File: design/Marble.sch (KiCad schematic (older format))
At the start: 20 parts

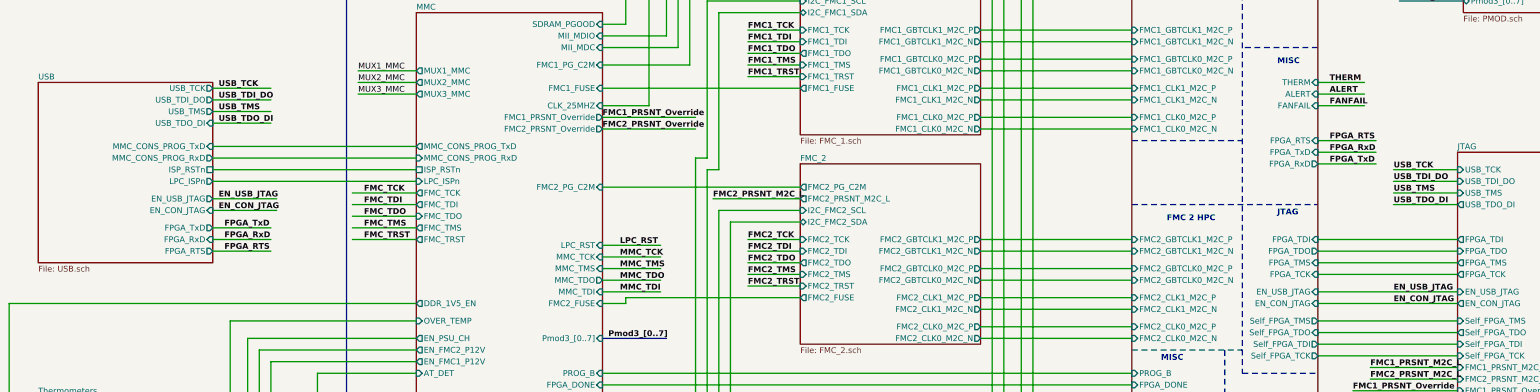
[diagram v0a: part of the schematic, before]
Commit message: buffering, solved ERC issues
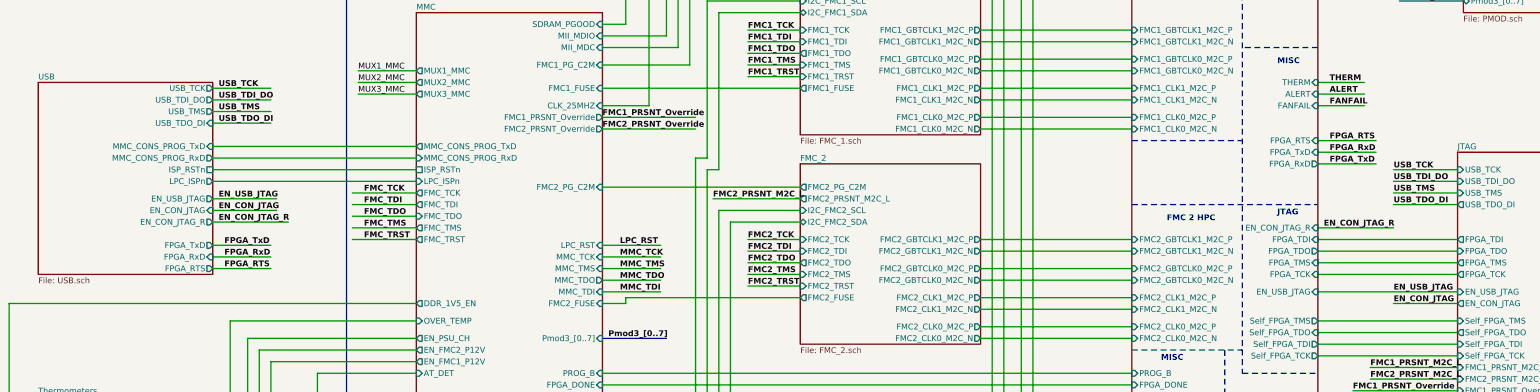
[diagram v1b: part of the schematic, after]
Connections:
- net labels added: EN_CON_JTAG_R
- wire segments 370 -> 372
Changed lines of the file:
@@
 $EndSheet
 $Sheet
-S 1950 7250 1500 1550
+S 1950 7250 1500 1650
 U 5C16C03C
 F0 "USB" 50
@@
 F9 "MMC_CONS_PROG_RxD" O R 3450 7900 50
 F10 "EN_CON_JTAG" I R 3450 8350 50
-F11 "FPGA_TxD" O R 3450 8500 50
-F12 "FPGA_RxD" I R 3450 8600 50
-F13 "FPGA_RTS" O R 3450 8700 50
+F11 "FPGA_TxD" O R 3450 8650 50
+F12 "FPGA_RxD" I R 3450 8750 50
+F13 "FPGA_RTS" O R 3450 8850 50
 F14 "ISP_RSTn" U R 3450 8000 50
+F15 "EN_CON_JTAG_R" O R 3450 8450 50
 $EndSheet
 Wire Wire Line
@@
 Wire Wire Line
 	12950 9050 14150 9050
-Wire Wire Line
-	12950 9150 14150 9150
 Text Label 6950 8650 0    50   ~ 10
 LPC_RST
@@
 Wire Wire Line
 	13450 7950 12950 7950
-Text Label 3550 8700 0    50   ~ 10
+Text Label 3550 8850 0    50   ~ 10
 FPGA_RTS
-Text Label 3550 8600 0    50   ~ 10
+Text Label 3550 8750 0    50   ~ 10
 FPGA_RxD
-Text Label 3550 8500 0    50   ~ 10
+Text Label 3550 8650 0    50   ~ 10
 FPGA_TxD
 Wire Wire Line
-	3950 8700 3450 8700
-Wire Wire Line
-	3950 8600 3450 8600
-Wire Wire Line
-	3950 8500 3450 8500
+	3950 8850 3450 8850
+Wire Wire Line
+	3950 8750 3450 8750
+Wire Wire Line
+	3950 8650 3450 8650
 Wire Wire Line
 	13400 9700 14150 9700
@@
 F58 "Self_FPGA_TDI" O R 12950 9500 50
 F59 "Self_FPGA_TCK" O R 12950 9600 50
-F60 "EN_CON_JTAG" I R 12950 9150 50
-F61 "EN_USB_JTAG" I R 12950 9050 50
-F62 "FPGA_RTS" I R 12950 7750 50
-F63 "FPGA_TxD" I R 12950 7850 50
-F64 "FPGA_RxD" O R 12950 7950 50
-F65 "RGMII_RXD[0..3]" I L 11350 4300 50
-F66 "RGMII_TXD[0..3]" I L 11350 4400 50
-F67 "RGMII_TX_EN" I L 11350 4500 50
-F68 "RGMII_TX_CLK" I L 11350 4600 50
-F69 "RGMII_RX_DV" I L 11350 4700 50
-F70 "RGMII_RX_CLK" I L 11350 4800 50
-F71 "SI570_CLK_P" I L 11350 3050 50
-F72 "SI570_CLK_N" I L 11350 3150 50
-F73 "QSFP1_MOD_SEL" O R 12950 14950 50
-F74 "QSFP1_RST" O R 12950 15050 50
-F75 "QSFP1_MOD_PRS" O R 12950 15150 50
-F76 "QSFP1_INT" I R 12950 15250 50
-F77 "QSFP1_LPMODE" O R 12950 15350 50
-F78 "QSFP2_MOD_SEL" O R 12950 12300 50
-F79 "QSFP2_RST" O R 12950 12400 50
-F80 "QSFP2_MOD_PRS" O R 12950 12500 50
-F81 "QSFP2_INT" I R 12950 12600 50
-F82 "QSFP2_LPMODE" O R 12950 12700 50
-F83 "QSFP1_TX_1_P" O R 12950 13150 50
-F84 "QSFP1_TX_1_N" O R 12950 13250 50
-F85 "QSFP1_RX_1_P" I R 12950 13350 50
-F86 "QSFP1_RX_1_N" I R 12950 13450 50
-F87 "QSFP1_TX_2_P" O R 12950 13600 50
-F88 "QSFP1_TX_2_N" O R 12950 13700 50
-F89 "QSFP1_RX_2_P" I R 12950 13800 50
-F90 "QSFP1_RX_2_N" I R 12950 13900 50
-F91 "QSFP1_TX_3_P" O R 12950 14050 50
-F92 "QSFP1_TX_3_N" O R 12950 14150 50
-F93 "QSFP1_RX_3_P" I R 12950 14250 50
-F94 "QSFP1_RX_3_N" I R 12950 14350 50
-F95 "QSFP1_TX_4_P" O R 12950 14500 50
-F96 "QSFP1_TX_4_N" O R 12950 14600 50
-F97 "QSFP1_RX_4_P" I R 12950 14700 50
-F98 "QSFP1_RX_4_N" I R 12950 14800 50
-F99 "QSFP2_TX_1_P" O R 12950 10500 50
-F100 "QSFP2_TX_1_N" O R 12950 10600 50
-F101 "QSFP2_RX_1_P" I R 12950 10700 50
-F102 "QSFP2_RX_1_N" I R 12950 10800 50
-F103 "QSFP2_TX_2_P" O R 12950 10950 50
-F104 "QSFP2_TX_2_N" O R 12950 11050 50
-F105 "QSFP2_RX_2_P" I R 12950 11150 50
-F106 "QSFP2_RX_2_N" I R 12950 11250 50
-F107 "QSFP2_TX_3_P" O R 12950 11400 50
-F108 "QSFP2_TX_3_N" O R 12950 11500 50
-F109 "QSFP2_RX_3_P" I R 12950 11600 50
-F110 "QSFP2_RX_3_N" I R 12950 11700 50
-F111 "QSFP2_TX_4_P" O R 12950 11850 50
-F112 "QSFP2_TX_4_N" O R 12950 11950 50
-F113 "QSFP2_RX_4_P" I R 12950 12050 50
-F114 "QSFP2_RX_4_N" I R 12950 12150 50
-F115 "FMC1_GBTCLK1_M2C_P" I L 11350 6800 50
-F116 "FMC1_GBTCLK1_M2C_N" I L 11350 6900 50
-F117 "FMC2_GBTCLK1_M2C_P" I L 11350 8600 50
-F118 "FMC2_GBTCLK1_M2C_N" I L 11350 8700 50
-F119 "MUX1_MMC" I L 11350 12250 50
-F120 "MUX2_MMC" I L 11350 12350 50
-F121 "MUX3_MMC" I L 11350 12450 50
-F122 "I2C_CLKMUX_SCL" I L 11350 5300 50
-F123 "I2C_CLKMUX_SDA" B L 11350 5400 50
-F124 "DDR3_DQ[32..63]" B R 12950 2300 50
-F125 "DDR3_DQS4_P" B R 12950 3500 50
-F126 "DDR3_DQS4_N" B R 12950 3600 50
-F127 "DDR3_DQS5_P" B R 12950 3700 50
-F128 "DDR3_DQS5_N" B R 12950 3800 50
-F129 "DDR3_DQS6_P" B R 12950 3900 50
-F130 "DDR3_DQS6_N" B R 12950 4000 50
-F131 "DDR3_DQS7_P" B R 12950 4100 50
-F132 "DDR3_DQS7_N" B R 12950 4200 50
-F133 "DDR3_DM[4..7]" B R 12950 2550 50
-F134 "DDR3_RAS_N" B R 12950 5250 50
-F135 "DDR3_CAS_N" B R 12950 5350 50
-F136 "DDR3_WE_N" B R 12950 5450 50
-F137 "DDR3_CS_N" B R 12950 5050 50
-F138 "DDR3_DQS0_P" B R 12950 2700 50
-F139 "DDR3_DQS0_N" B R 12950 2800 50
-F140 "DDR3_DQS1_P" B R 12950 2900 50
-F141 "DDR3_DQS1_N" B R 12950 3000 50
-F142 "DDR3_DQS2_P" B R 12950 3100 50
-F143 "DDR3_DQS2_N" B R 12950 3200 50
-F144 "DDR3_DQS3_P" B R 12950 3300 50
-F145 "DDR3_DQS3_N" B R 12950 3400 50
-F146 "DDR3_DM[0..3]" B R 12950 2450 50
-F147 "DDR3_DQ[0..31]" B R 12950 2200 50
-F148 "VREF_DDR3" I R 12950 5600 50
-F149 "SI570_OE" O L 11350 5600 50
-F150 "XRP_POWER_GOOD" I L 11350 12000 50
+F60 "EN_USB_JTAG" I R 12950 9050 50
+F61 "FPGA_RTS" I R 12950 7750 50
+F62 "FPGA_TxD" I R 12950 7850 50
+F63 "FPGA_RxD" O R 12950 7950 50
+F64 "RGMII_RXD[0..3]" I L 11350 4300 50
+F65 "RGMII_TXD[0..3]" I L 11350 4400 50
+F66 "RGMII_TX_EN" I L 11350 4500 50
+F67 "RGMII_TX_CLK" I L 11350 4600 50
+F68 "RGMII_RX_DV" I L 11350 4700 50
+F69 "RGMII_RX_CLK" I L 11350 4800 50
+F70 "SI570_CLK_P" I L 11350 3050 50
+F71 "SI570_CLK_N" I L 11350 3150 50
+F72 "QSFP1_MOD_SEL" O R 12950 14950 50
+F73 "QSFP1_RST" O R 12950 15050 50
+F74 "QSFP1_MOD_PRS" O R 12950 15150 50
+F75 "QSFP1_INT" I R 12950 15250 50
+F76 "QSFP1_LPMODE" O R 12950 15350 50
+F77 "QSFP2_MOD_SEL" O R 12950 12300 50
+F78 "QSFP2_RST" O R 12950 12400 50
+F79 "QSFP2_MOD_PRS" O R 12950 12500 50
+F80 "QSFP2_INT" I R 12950 12600 50
+F81 "QSFP2_LPMODE" O R 12950 12700 50
+F82 "QSFP1_TX_1_P" O R 12950 13150 50
+F83 "QSFP1_TX_1_N" O R 12950 13250 50
+F84 "QSFP1_RX_1_P" I R 12950 13350 50
+F85 "QSFP1_RX_1_N" I R 12950 13450 50
+F86 "QSFP1_TX_2_P" O R 12950 13600 50
+F87 "QSFP1_TX_2_N" O R 12950 13700 50
+F88 "QSFP1_RX_2_P" I R 12950 13800 50
+F89 "QSFP1_RX_2_N" I R 12950 13900 50
+F90 "QSFP1_TX_3_P" O R 12950 14050 50
+F91 "QSFP1_TX_3_N" O R 12950 14150 50
+F92 "QSFP1_RX_3_P" I R 12950 14250 50
+F93 "QSFP1_RX_3_N" I R 12950 14350 50
+F94 "QSFP1_TX_4_P" O R 12950 14500 50
+F95 "QSFP1_TX_4_N" O R 12950 14600 50
+F96 "QSFP1_RX_4_P" I R 12950 14700 50
+F97 "QSFP1_RX_4_N" I R 12950 14800 50
+F98 "QSFP2_TX_1_P" O R 12950 10500 50
+F99 "QSFP2_TX_1_N" O R 12950 10600 50
+F100 "QSFP2_RX_1_P" I R 12950 10700 50
+F101 "QSFP2_RX_1_N" I R 12950 10800 50
+F102 "QSFP2_TX_2_P" O R 12950 10950 50
+F103 "QSFP2_TX_2_N" O R 12950 11050 50
+F104 "QSFP2_RX_2_P" I R 12950 11150 50
+F105 "QSFP2_RX_2_N" I R 12950 11250 50
+F106 "QSFP2_TX_3_P" O R 12950 11400 50
+F107 "QSFP2_TX_3_N" O R 12950 11500 50
+F108 "QSFP2_RX_3_P" I R 12950 11600 50
+F109 "QSFP2_RX_3_N" I R 12950 11700 50
+F110 "QSFP2_TX_4_P" O R 12950 11850 50
+F111 "QSFP2_TX_4_N" O R 12950 11950 50
+F112 "QSFP2_RX_4_P" I R 12950 12050 50
+F113 "QSFP2_RX_4_N" I R 12950 12150 50
+F114 "FMC1_GBTCLK1_M2C_P" I L 11350 6800 50
+F115 "FMC1_GBTCLK1_M2C_N" I L 11350 6900 50
+F116 "FMC2_GBTCLK1_M2C_P" I L 11350 8600 50
+F117 "FMC2_GBTCLK1_M2C_N" I L 11350 8700 50
+F118 "MUX1_MMC" I L 11350 12250 50
+F119 "MUX2_MMC" I L 11350 12350 50
+F120 "MUX3_MMC" I L 11350 12450 50
+F121 "I2C_CLKMUX_SCL" I L 11350 5300 50
+F122 "I2C_CLKMUX_SDA" B L 11350 5400 50
+F123 "DDR3_DQ[32..63]" B R 12950 2300 50
+F124 "DDR3_DQS4_P" B R 12950 3500 50
+F125 "DDR3_DQS4_N" B R 12950 3600 50
+F126 "DDR3_DQS5_P" B R 12950 3700 50
+F127 "DDR3_DQS5_N" B R 12950 3800 50
+F128 "DDR3_DQS6_P" B R 12950 3900 50
+F129 "DDR3_DQS6_N" B R 12950 4000 50
+F130 "DDR3_DQS7_P" B R 12950 4100 50
+F131 "DDR3_DQS7_N" B R 12950 4200 50
+F132 "DDR3_DM[4..7]" B R 12950 2550 50
+F133 "DDR3_RAS_N" B R 12950 5250 50
+F134 "DDR3_CAS_N" B R 12950 5350 50
+F135 "DDR3_WE_N" B R 12950 5450 50
+F136 "DDR3_CS_N" B R 12950 5050 50
+F137 "DDR3_DQS0_P" B R 12950 2700 50
+F138 "DDR3_DQS0_N" B R 12950 2800 50
+F139 "DDR3_DQS1_P" B R 12950 2900 50
+F140 "DDR3_DQS1_N" B R 12950 3000 50
+F141 "DDR3_DQS2_P" B R 12950 3100 50
+F142 "DDR3_DQS2_N" B R 12950 3200 50
+F143 "DDR3_DQS3_P" B R 12950 3300 50
+F144 "DDR3_DQS3_N" B R 12950 3400 50
+F145 "DDR3_DM[0..3]" B R 12950 2450 50
+F146 "DDR3_DQ[0..31]" B R 12950 2200 50
+F147 "VREF_DDR3" I R 12950 5600 50
+F148 "SI570_OE" O L 11350 5600 50
+F149 "XRP_POWER_GOOD" I L 11350 12000 50
+F150 "EN_CON_JTAG_R" I R 12950 8500 50
 $EndSheet
 Wire Notes Line
@@
 	4750 10400 5200 10400
 Connection ~ 4750 11650
+Text Label 3500 8450 0    50   ~ 10
+EN_CON_JTAG_R
+Wire Wire Line
+	3450 8450 4100 8450
+Text Label 13000 8500 0    50   ~ 10
+EN_CON_JTAG_R
+Wire Wire Line
+	12950 8500 13600 8500
+Wire Wire Line
+	13600 9150 14150 9150
 $EndSCHEMATC

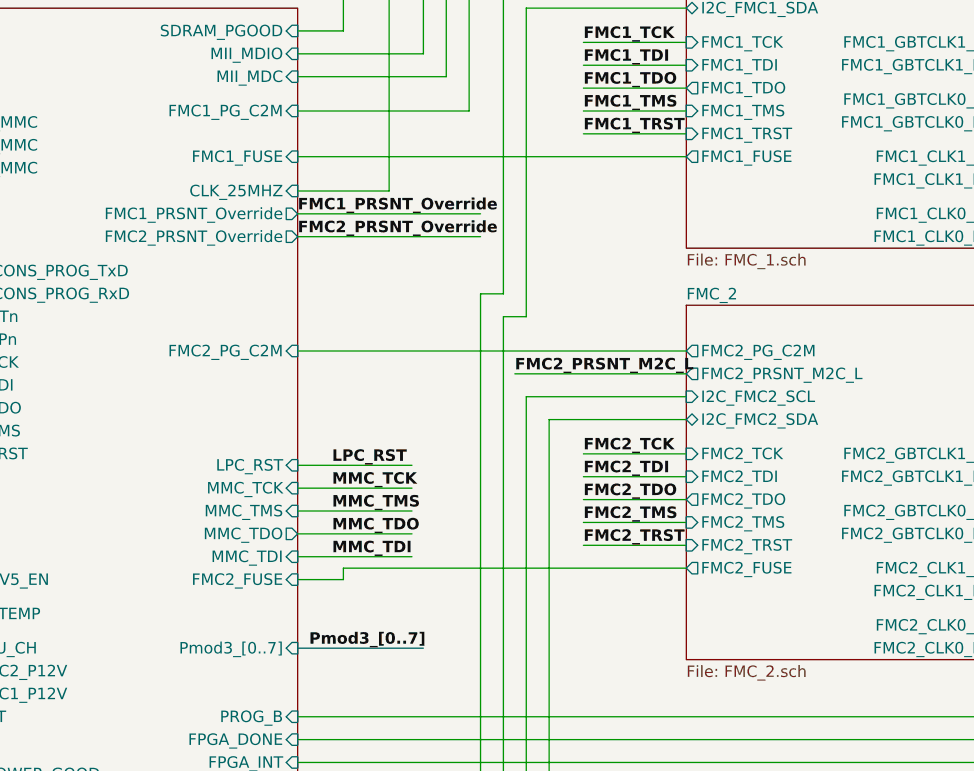
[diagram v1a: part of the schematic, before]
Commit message: VIO_B_M2Cs connected to MMC's adc inputs
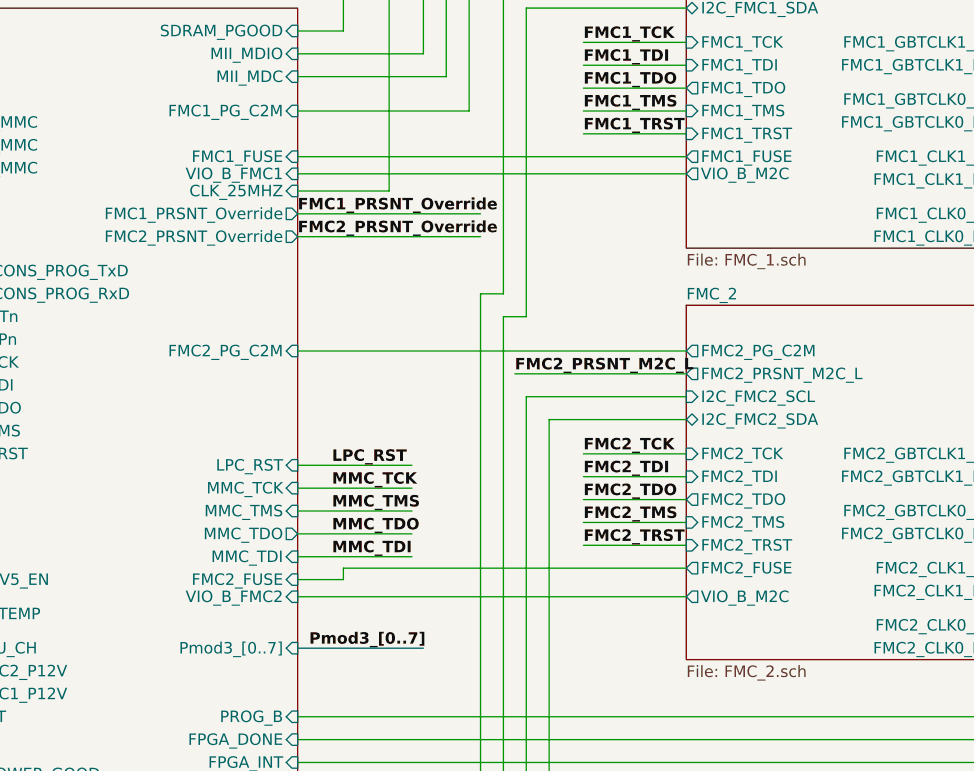
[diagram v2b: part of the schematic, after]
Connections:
- wire segments 372 -> 374
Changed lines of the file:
@@
 F18 "FMC1_GBTCLK1_M2C_P" O R 10050 6800 50
 F19 "FMC1_GBTCLK1_M2C_N" O R 10050 6900 50
+F20 "VIO_B_M2C" O L 8500 7375 50
 $EndSheet
 $Comp
@@
 F49 "XRP_POWER_GOOD" I L 5200 10000 50
 F50 "I2C_FPGA_SW_RST" O L 5200 10400 50
+F51 "VIO_B_FMC1" I R 6800 7375 50
+F52 "VIO_B_FMC2" I R 6800 9225 50
 $EndSheet
 Text Label 6800 7550 0    50   ~ 10
@@
 F18 "FMC2_GBTCLK1_M2C_P" O R 10050 8600 50
 F19 "FMC2_GBTCLK1_M2C_N" O R 10050 8700 50
+F20 "VIO_B_M2C" O L 8500 9225 50
 $EndSheet
 Wire Wire Line
@@
 Wire Wire Line
 	13600 9150 14150 9150
+Wire Wire Line
+	8500 9225 6800 9225
+Wire Wire Line
+	6800 7375 8500 7375
 $EndSCHEMATC
